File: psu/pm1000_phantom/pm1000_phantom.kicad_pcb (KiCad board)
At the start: 2 copper layers, 27.9 x 41.3 mm, 17 parts, among them J1 48V in, J10 power led, J2 Phantom A switch, J3 Phantom B switch, J4 Phantom A led, J5 Phantom B led, J6 Chan A out, J7 Chan A int, J8 Chan B out, J9 Chan B int

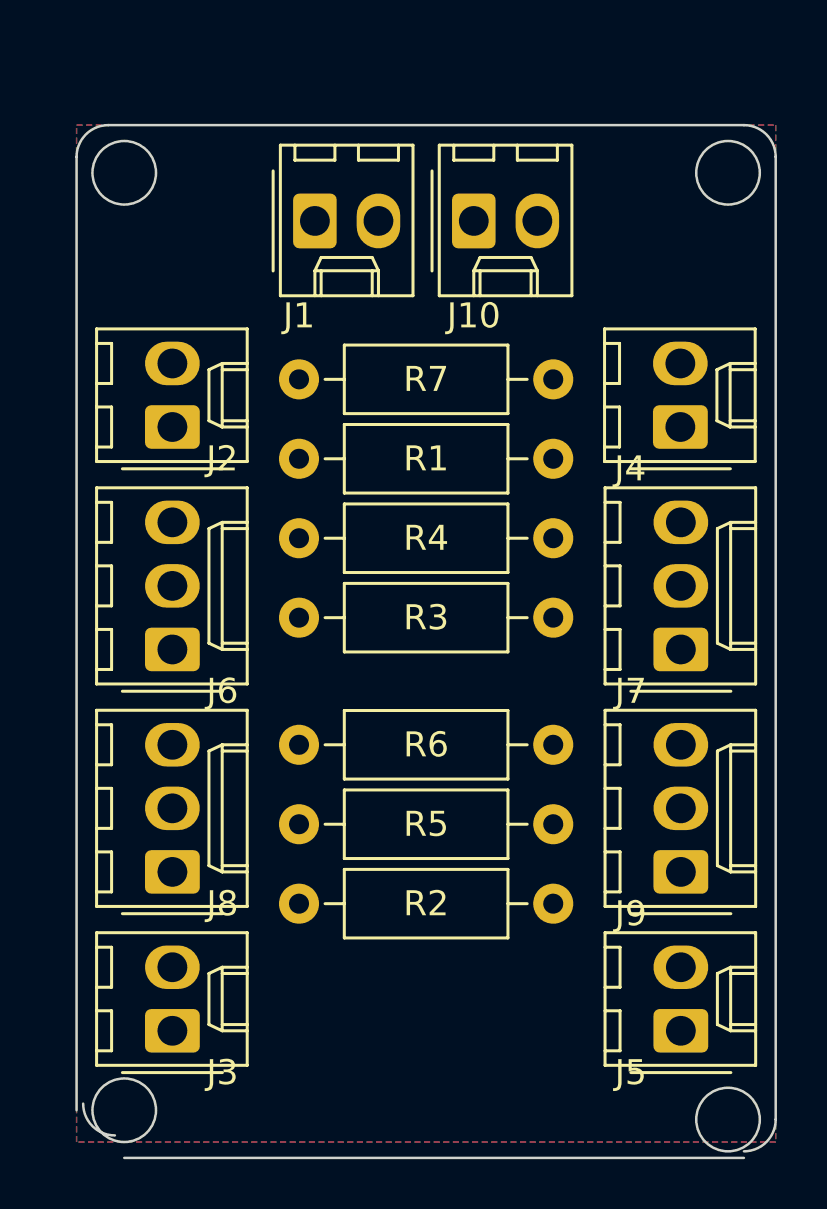
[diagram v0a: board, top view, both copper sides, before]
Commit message: update phantom board
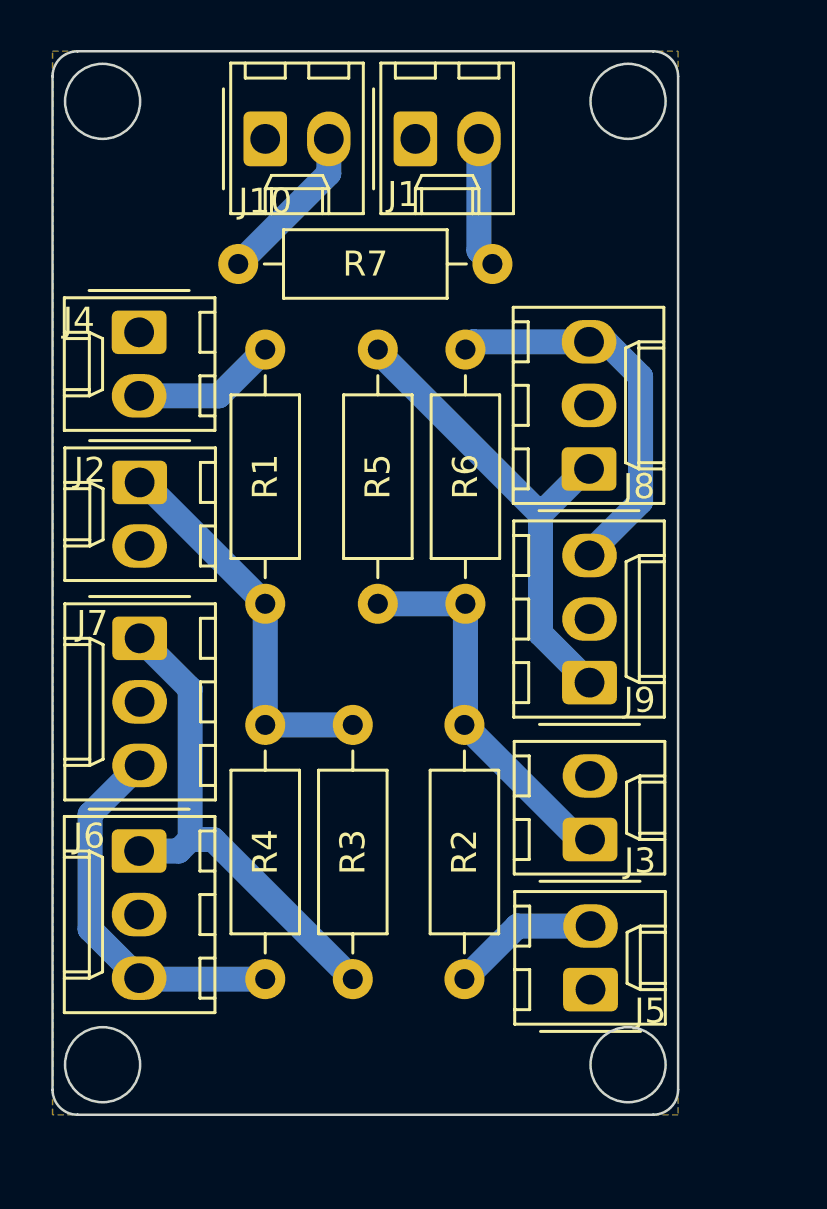
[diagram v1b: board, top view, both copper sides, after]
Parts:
- moved J8 23.2 mm to (81.4, 121.7)
- moved J4 22.0 mm to (63.5, 116.2), turned to -90 degrees
- moved J7 21.6 mm to (63.5, 128.5), turned to -90 degrees
- moved R4 21.0 mm to (68.5, 142.1), turned to 90 degrees
- moved R5 20.2 mm to (73.0, 116.9), turned to -90 degrees
- moved J3 18.4 mm to (81.5, 136.5)
- moved R3 16.5 mm to (72.0, 142.1), turned to 90 degrees
- moved R6 16.2 mm to (76.5, 116.9), turned to -90 degrees
- moved R1 12.3 mm to (68.5, 116.9), turned to -90 degrees
- moved R7 9.00 mm to (77.6, 113.5), turned to 180 degrees
- moved J10 8.96 mm to (68.5, 108.5)
- moved J9 8.40 mm to (81.5, 130.2)
- moved J6 8.16 mm to (63.5, 137.0), turned to -90 degrees
- moved J1 5.18 mm to (74.5, 108.5)
- moved R2 4.66 mm to (76.5, 142.1), turned to 90 degrees
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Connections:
- J1 pad 1: +48V -> GND
- J1 pad 2: GND -> +48V
- J10 pad 1: Net-(J10-Pad1) -> GND
- J10 pad 2: GND -> Net-(R7-Pad2)
- J2 pad 1: +48V -> +48 switched A
- J2 pad 2: +48 switched A -> +48V
- J3 pad 1: +48V -> +48 switched B
- J3 pad 2: +48 switched B -> +48V
- J4 pad 1: Net-(J4-Pad1) -> GND
- J4 pad 2: GND -> Net-(R1-Pad1)
- J5 pad 1: Net-(J5-Pad1) -> GND
- J5 pad 2: GND -> Net-(R2-Pad1)
- R1 pad 1: Net-(J4-Pad1) -> Net-(R1-Pad1)
- R2 pad 1: Net-(J5-Pad1) -> Net-(R2-Pad1)
- R7 pad 2: Net-(J10-Pad1) -> Net-(R7-Pad2)
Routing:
- net Net-(J6-Pad1): track 0.00 -> 19.9 mm
- net Net-(J8-Pad1): track 0.00 -> 19.5 mm
- net Net-(J8-Pad3): track 0.00 -> 15.7 mm
- net +48 switched A: track 0.00 -> 15.4 mm
- net +48 switched B: track 0.00 -> 15.3 mm
- net Net-(J6-Pad3): track 0.00 -> 15.2 mm
- net Net-(R7-Pad2): track 0.00 -> 6.50 mm
- net Net-(R2-Pad1): track 0.00 -> 5.92 mm
- net Net-(R1-Pad1): track 0.00 -> 5.81 mm
- net +48V: track 0.00 -> 5.22 mm
- added copper zone on B.Cu, net +48V
- removed copper zone on B.Cu, net GND
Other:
- board size 27.9 x 41.3 mm -> 25 x 42.5 mm

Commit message: update boms with (some) mouser part numbers add 100n capacitors add power leds add frontpanel power led connector to psu board
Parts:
- J1: value 48V in -> 2 pin Molex
- J10: value power led -> 2 pin Molex
- J2: value Phantom A switch -> 2 pin Molex
- J3: value Phantom B switch -> 2 pin Molex
- J4: value Phantom A led -> 2 pin Molex
- J5: value Phantom B led -> 2 pin Molex
- J6: value Chan A out -> 3 pin Molex
- J7: value Chan A int -> 3 pin Molex
- J8: value Chan B out -> 3 pin Molex
- J9: value Chan B int -> 3 pin Molex

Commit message: route phantom pcb
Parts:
- J1, J10, J2, J3, J4, J5: value 2 pin Molex -> 2 pin 2,54mm Molex
- J6, J7, J8, J9: value 3 pin Molex -> 3 pin 2,54mm Molex
- moved J9 5.23 mm to (81.5, 125.0), turned to -90 degrees
- moved J8 5.19 mm to (81.5, 116.5), turned to -90 degrees
- moved J6 4.83 mm to (63.5, 141.8), turned to 90 degrees
- moved J7 4.83 mm to (63.5, 133.3), turned to 90 degrees
- moved J5 3.02 mm to (81.5, 139.5), turned to -90 degrees
- moved J3 3.00 mm to (81.5, 133.5), turned to -90 degrees
- moved J2 2.52 mm to (63.5, 124.8), turned to 90 degrees
- moved J4 2.52 mm to (63.5, 118.8), turned to 90 degrees
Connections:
- J7 pad 2: unconnected-(J7-Pad2) -> GND
- J9 pad 2: unconnected-(J9-Pad2) -> GND
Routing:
- net Net-(J6-Pad3): track 15.2 -> 19.6 mm
- net Net-(J8-Pad1): track 19.5 -> 22.4 mm
- net Net-(J8-Pad3): track 15.7 -> 17.9 mm
- net Net-(J6-Pad1): track 19.9 -> 21.6 mm
- net +48 switched B: track 15.3 -> 14.1 mm
- net +48 switched A: track 15.4 -> 14.3 mm
- net Net-(J5-Pad2): track 5.92 -> 5.06 mm
